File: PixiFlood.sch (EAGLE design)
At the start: 59 parts, among them IC1 74LVC1G125DBV, IC2 WS2811SOP8, IC3 BD9G401EFJ-ME2, IC4 AL-8861SOT89-5, IC5 AL-8861SOT89-5, IC6 AL-8861SOT89-5, Q1 BC847BC847, Q2 BC847BC847, Q3 BC847BC847, T1 ST06ECH350V-06P

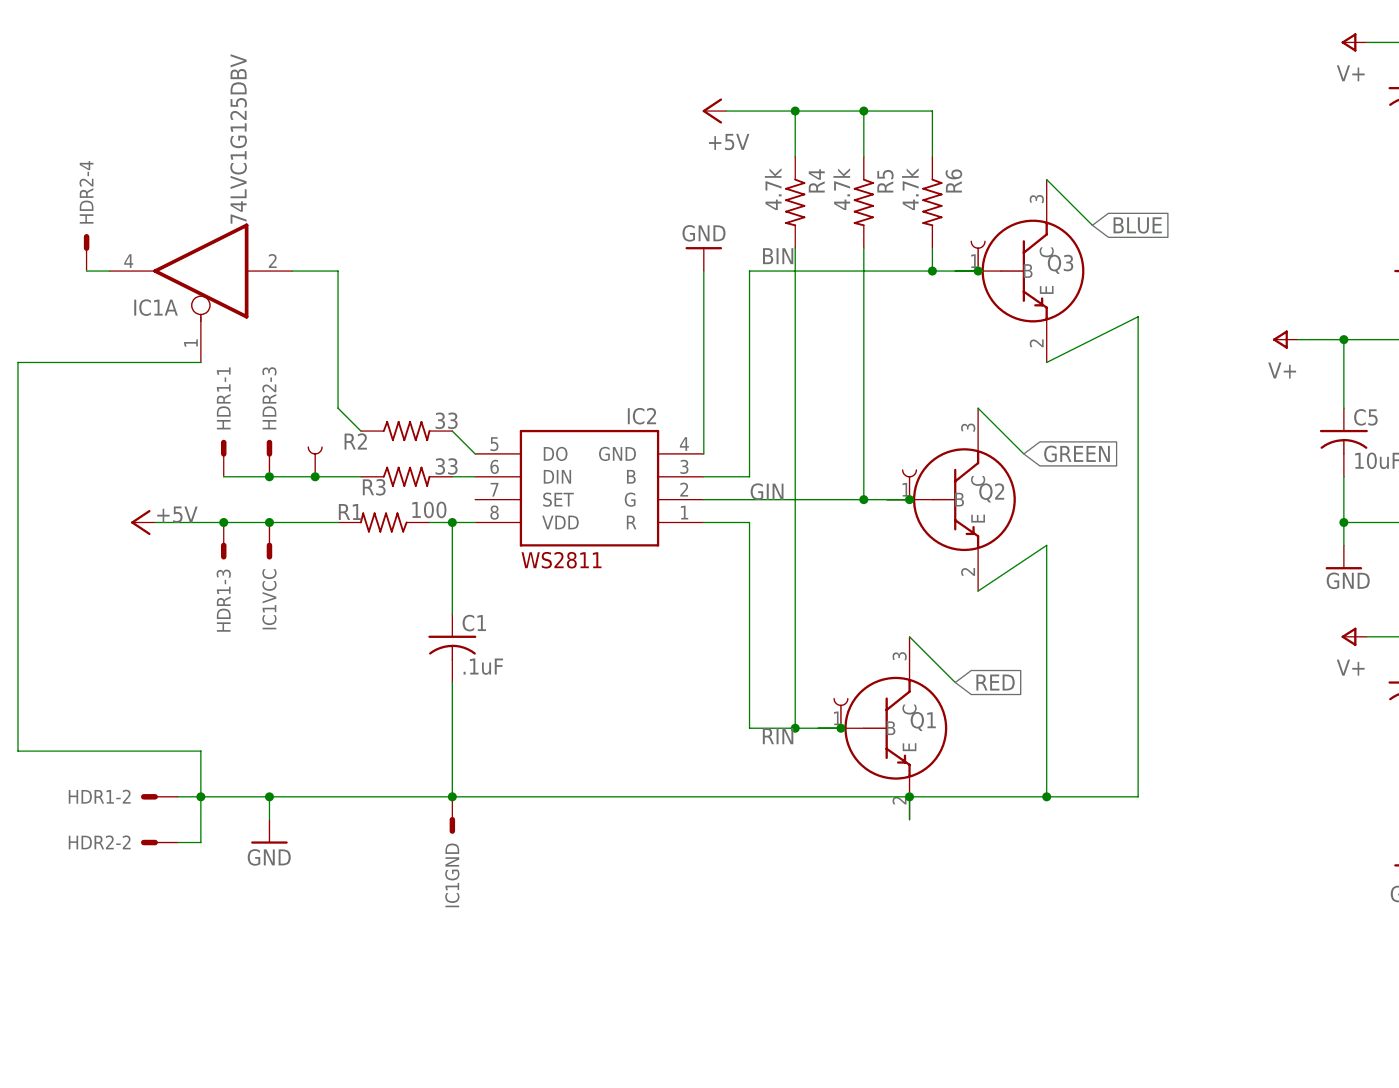
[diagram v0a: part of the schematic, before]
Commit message: Cleaned up transistors
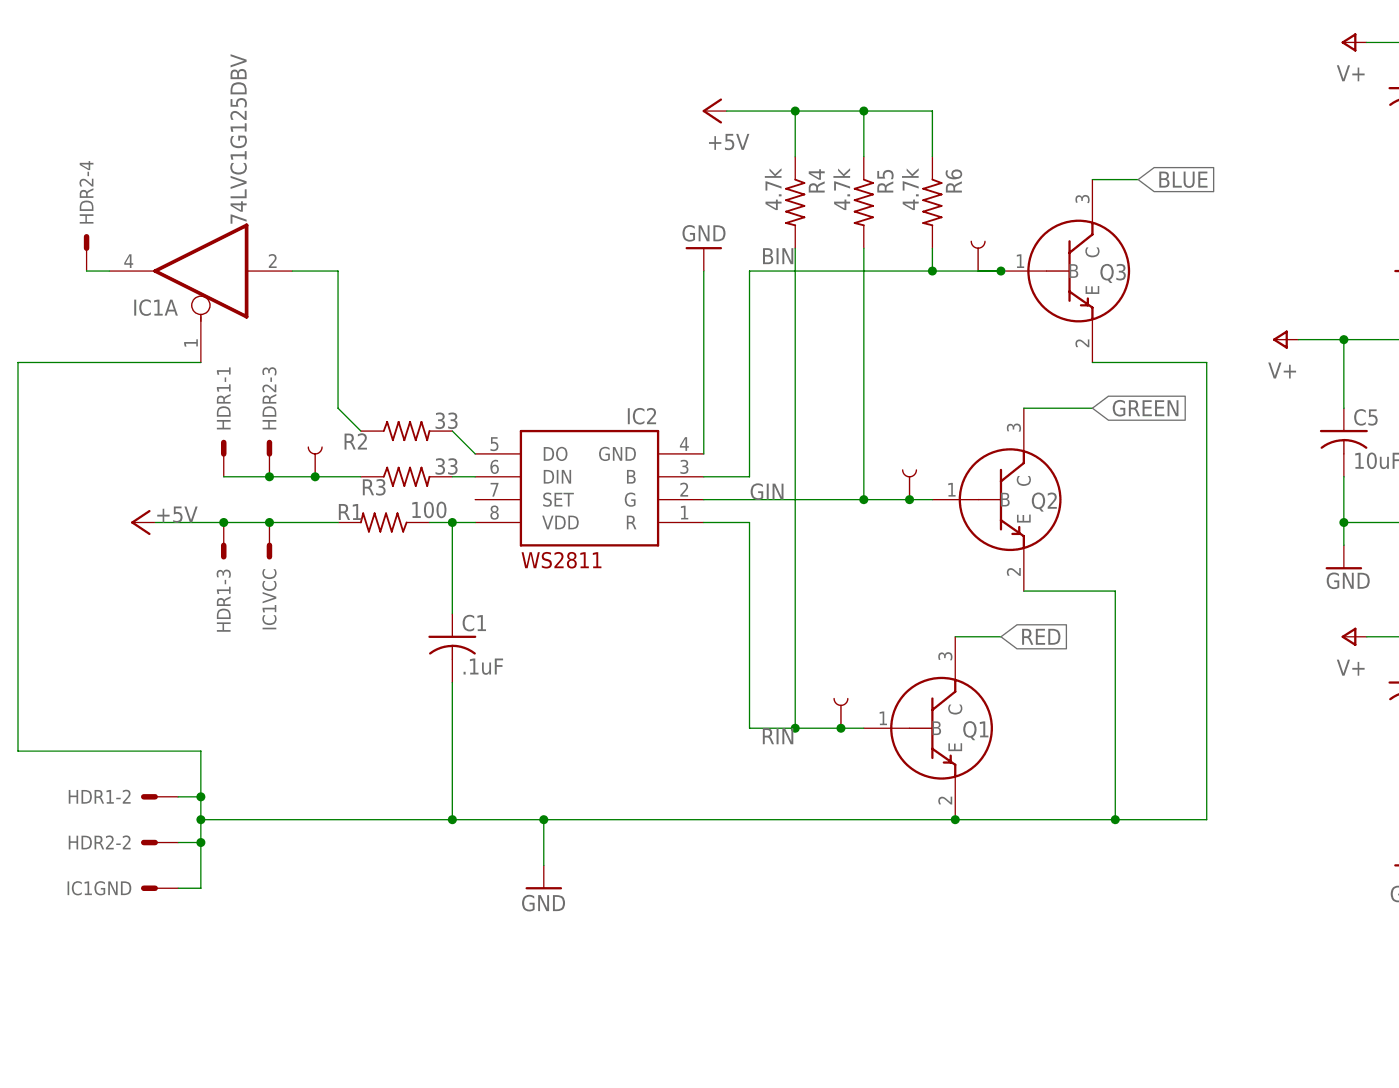
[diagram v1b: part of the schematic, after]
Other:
- moved on the sheet: IC1GND, Q1, Q2, Q3

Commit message: Changed Connector
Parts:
- TP11, TP12, TP2, TP20, TP21, TP22, TP23, TP3, TP5, TP6, TP7, TP8: device headers:TEST_PINTP-2 -> headers:TEST_PINTP-1

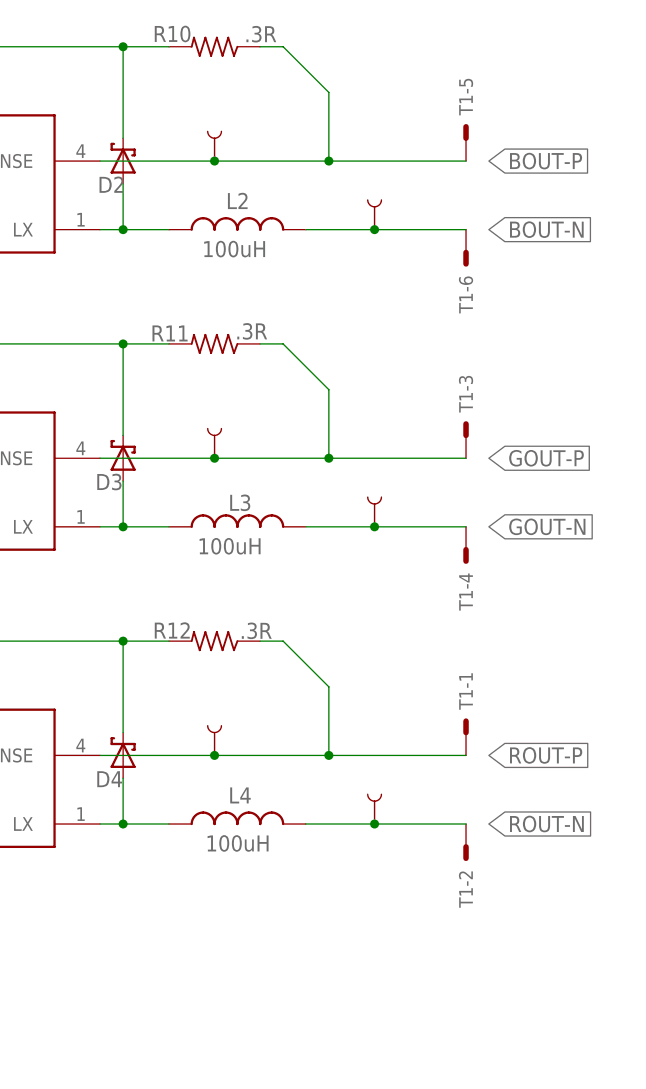
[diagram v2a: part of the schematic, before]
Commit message: added adpater boards and changed pinout on led
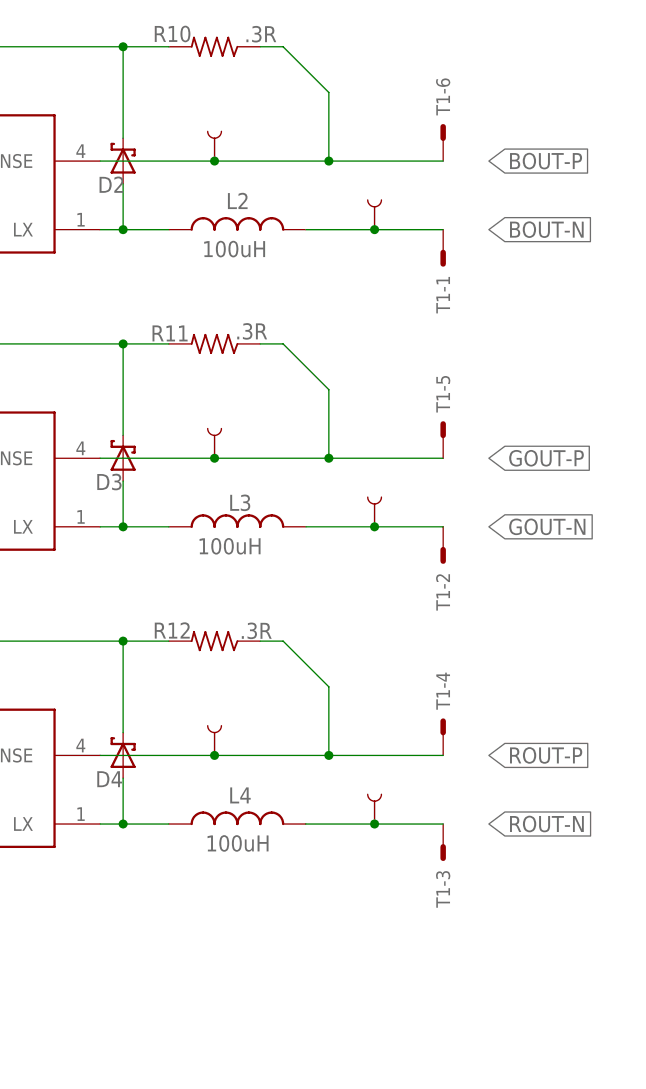
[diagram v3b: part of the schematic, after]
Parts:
- T1: value ST06ECH350V-06P -> (none); device connectors:ST06ECH350V-06P -> headers:M06SIP
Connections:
- net BOUT-N: now also T1-1.S; no longer T1-6.S
- net BOUT-P: now also T1-6.S; no longer T1-5.S
- net GOUT-N: now also T1-2.S; no longer T1-4.S
- net GOUT-P: now also T1-5.S; no longer T1-3.S
- net ROUT-N: now also T1-3.S; no longer T1-2.S
- net ROUT-P: now also T1-4.S; no longer T1-1.S
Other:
- moved on the sheet: T1-1, T1-2, T1-3, T1-4, T1-5, T1-6
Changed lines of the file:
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@@
 <?xml version="1.0" encoding="utf-8"?>
 <!DOCTYPE eagle SYSTEM "eagle.dtd">
-<eagle version="9.4.1">
+<eagle version="9.4.2">
 <drawing>
 <settings>
@@
 <part name="IC5" library="drivers" deviceset="AL-8861" device="SOT89-5"/>
 <part name="IC4" library="drivers" deviceset="AL-8861" device="SOT89-5"/>
-<part name="T1" library="connectors" deviceset="ST06" device="ECH350V-06P"/>
+<part name="T1" library="headers" deviceset="M06" device="SIP"/>
 </parts>
 <sheets>
@@
 <attribute name="NAME" x="305.308" y="110.998" size="1.27" layer="95" rot="R180" align="bottom-right"/>
 </instance>
-<instance part="T1" gate="-1" x="363.22" y="50.8" smashed="yes" rot="R90">
-<attribute name="NAME" x="363.982" y="53.34" size="1.524" layer="95" rot="R90"/>
-</instance>
-<instance part="T1" gate="-2" x="363.22" y="38.1" smashed="yes" rot="R270">
-<attribute name="NAME" x="362.458" y="35.56" size="1.524" layer="95" rot="R270"/>
-</instance>
-<instance part="T1" gate="-3" x="363.22" y="83.82" smashed="yes" rot="R90">
-<attribute name="NAME" x="363.982" y="86.36" size="1.524" layer="95" rot="R90"/>
-</instance>
-<instance part="T1" gate="-4" x="363.22" y="71.12" smashed="yes" rot="R270">
-<attribute name="NAME" x="362.458" y="68.58" size="1.524" layer="95" rot="R270"/>
-</instance>
-<instance part="T1" gate="-5" x="363.22" y="116.84" smashed="yes" rot="R90">
-<attribute name="NAME" x="363.982" y="119.38" size="1.524" layer="95" rot="R90"/>
-</instance>
-<instance part="T1" gate="-6" x="363.22" y="104.14" smashed="yes" rot="R270">
-<attribute name="NAME" x="362.458" y="101.6" size="1.524" layer="95" rot="R270"/>
+<instance part="T1" gate="-1" x="360.68" y="104.14" smashed="yes" rot="R270">
+<attribute name="NAME" x="359.918" y="101.6" size="1.524" layer="95" rot="R270"/>
+</instance>
+<instance part="T1" gate="-2" x="360.68" y="71.12" smashed="yes" rot="R270">
+<attribute name="NAME" x="359.918" y="68.58" size="1.524" layer="95" rot="R270"/>
+</instance>
+<instance part="T1" gate="-3" x="360.68" y="38.1" smashed="yes" rot="R270">
+<attribute name="NAME" x="359.918" y="35.56" size="1.524" layer="95" rot="R270"/>
+</instance>
+<instance part="T1" gate="-4" x="360.68" y="50.8" smashed="yes" rot="R90">
+<attribute name="NAME" x="361.442" y="53.34" size="1.524" layer="95" rot="R90"/>
+</instance>
+<instance part="T1" gate="-5" x="360.68" y="83.82" smashed="yes" rot="R90">
+<attribute name="NAME" x="361.442" y="86.36" size="1.524" layer="95" rot="R90"/>
+</instance>
+<instance part="T1" gate="-6" x="360.68" y="116.84" smashed="yes" rot="R90">
+<attribute name="NAME" x="361.442" y="119.38" size="1.524" layer="95" rot="R90"/>
 </instance>
 </instances>
@@
 <pinref part="IC4" gate="G$1" pin="ISENSE"/>
 <wire x1="335.28" y1="114.3" x2="322.58" y2="114.3" width="0.1524" layer="91"/>
-<wire x1="347.98" y1="114.3" x2="363.22" y2="114.3" width="0.1524" layer="91"/>
+<wire x1="347.98" y1="114.3" x2="360.68" y2="114.3" width="0.1524" layer="91"/>
 <junction x="347.98" y="114.3"/>
-<pinref part="T1" gate="-5" pin="S"/>
+<pinref part="T1" gate="-6" pin="S"/>
 </segment>
 </net>
@@
 <wire x1="342.9" y1="93.98" x2="347.98" y2="88.9" width="0.1524" layer="91"/>
 <pinref part="IC5" gate="G$1" pin="ISENSE"/>
-<wire x1="347.98" y1="81.28" x2="363.22" y2="81.28" width="0.1524" layer="91"/>
+<wire x1="347.98" y1="81.28" x2="360.68" y2="81.28" width="0.1524" layer="91"/>
 <junction x="347.98" y="81.28"/>
-<pinref part="T1" gate="-3" pin="S"/>
+<pinref part="T1" gate="-5" pin="S"/>
 </segment>
 </net>
@@
 <wire x1="345.44" y1="73.66" x2="353.06" y2="73.66" width="0.1524" layer="91"/>
 <pinref part="TP2" gate="G$1" pin="1"/>
-<wire x1="353.06" y1="73.66" x2="363.22" y2="73.66" width="0.1524" layer="91"/>
+<wire x1="353.06" y1="73.66" x2="360.68" y2="73.66" width="0.1524" layer="91"/>
 <junction x="353.06" y="73.66"/>
-<pinref part="T1" gate="-4" pin="S"/>
+<pinref part="T1" gate="-2" pin="S"/>
 </segment>
 </net>
@@
 <label x="365.76" y="106.68" size="1.778" layer="95" xref="yes"/>
 <pinref part="TP3" gate="G$1" pin="1"/>
-<wire x1="353.06" y1="106.68" x2="363.22" y2="106.68" width="0.1524" layer="91"/>
+<wire x1="353.06" y1="106.68" x2="360.68" y2="106.68" width="0.1524" layer="91"/>
 <junction x="353.06" y="106.68"/>
-<pinref part="T1" gate="-6" pin="S"/>
+<pinref part="T1" gate="-1" pin="S"/>
 </segment>
 </net>
@@
 <pinref part="IC6" gate="G$1" pin="ISENSE"/>
 <wire x1="322.58" y1="48.26" x2="335.28" y2="48.26" width="0.1524" layer="91"/>
-<wire x1="347.98" y1="48.26" x2="363.22" y2="48.26" width="0.1524" layer="91"/>
+<wire x1="347.98" y1="48.26" x2="360.68" y2="48.26" width="0.1524" layer="91"/>
 <junction x="347.98" y="48.26"/>
-<pinref part="T1" gate="-1" pin="S"/>
+<pinref part="T1" gate="-4" pin="S"/>
 </segment>
 </net>
@@
 <label x="365.76" y="40.64" size="1.778" layer="95" xref="yes"/>
 <pinref part="TP1" gate="G$1" pin="1"/>
-<wire x1="353.06" y1="40.64" x2="363.22" y2="40.64" width="0.1524" layer="91"/>
+<pinref part="T1" gate="-3" pin="S"/>
+<wire x1="353.06" y1="40.64" x2="360.68" y2="40.64" width="0.1524" layer="91"/>
 <junction x="353.06" y="40.64"/>
-<pinref part="T1" gate="-2" pin="S"/>
-</segment>
-</net>
+</segment>
+</net>
